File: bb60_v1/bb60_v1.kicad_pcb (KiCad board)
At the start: 2 copper layers, 281 x 94.4 mm, 145 parts, among them J1 Conn_01x04, SW1 SW_Push, SW2 SW_Push, U1 STM32F072CBTx, U2 XC6206PxxxMR, U3 USBLC6-2SC6

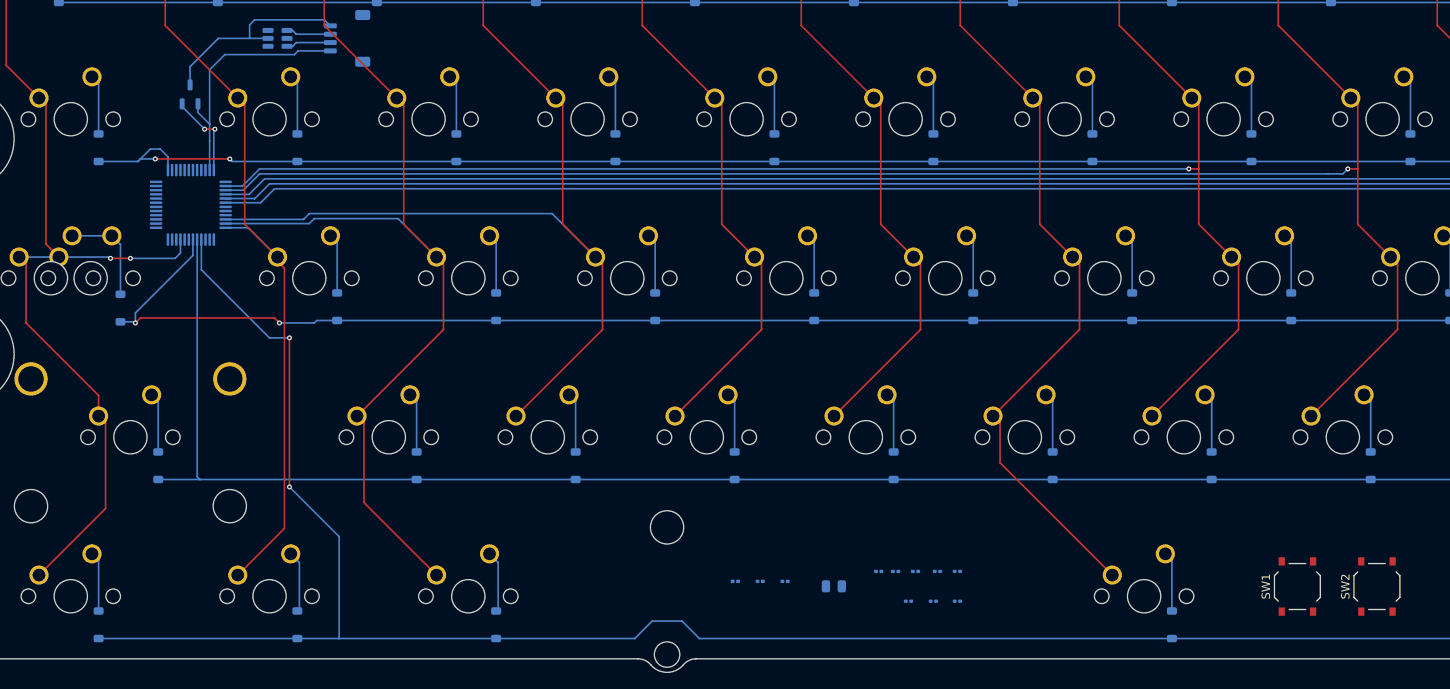
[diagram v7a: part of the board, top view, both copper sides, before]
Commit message: finished row/column traces
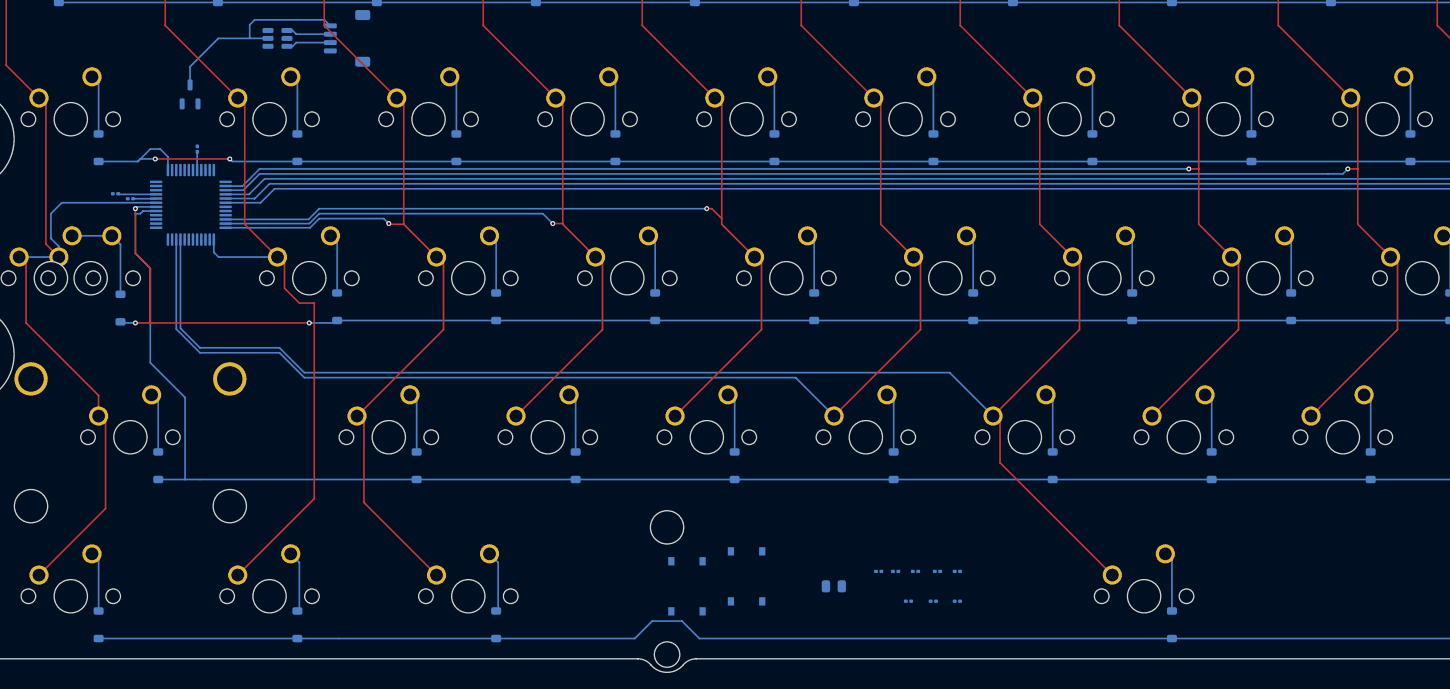
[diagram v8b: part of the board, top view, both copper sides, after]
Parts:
- SW1, SW2: moved to B.Cu
- moved R2 88.3 mm to (92.9, 107.0)
- moved R3 87.6 mm to (91.1, 106.4)
- moved R1 87.4 mm to (100.9, 101.0), turned to -90 degrees
- moved SW2 75.5 mm to (166.7, 152.2)
- moved SW1 73.1 mm to (159.5, 153.4)
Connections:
- U1 pad 10: /COL3 -> /COL4
- U1 pad 11: /COL2 -> /COL3
- U1 pad 12: /COL1 -> /COL2
- U1 pad 13: /COL6 -> /COL1
- U1 pad 14: /COL5 -> unconnected-(U1-PA4-Pad14)
- U1 pad 17: /ROW3 -> unconnected-(U1-PA7-Pad17)
- U1 pad 18: /ROW2 -> unconnected-(U1-PB0-Pad18)
- U1 pad 21: /COL0 -> /COL6
- U1 pad 22: unconnected-(U1-PB11-Pad22) -> /COL5
- U1 pad 29: unconnected-(U1-PA8-Pad29) -> /ROW3
- U1 pad 30: unconnected-(U1-PA9-Pad30) -> /ROW2
- U1 pad 31: unconnected-(U1-PA10-Pad31) -> /COL0
- U1 pad 43: /COL4 -> unconnected-(U1-PB7-Pad43)
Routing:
- net /COL6: track 92.7 -> 205.0 mm
- net /COL5: track 67.7 -> 161.5 mm
- net /COL4: track 67.7 -> 128.2 mm, vias 0 -> 1
- net /ROW4: track 316.7 -> 260.6 mm, vias 2 -> 0
- net GND: track 30.4 -> 0.00 mm
- net +3.3V: track 10.3 -> 0.00 mm, vias 2 -> 0
- net /ROW3: track 283.5 -> 291.6 mm
- net /COL1: track 92.4 -> 98.2 mm
- net /COL3: track 114.5 -> 109.1 mm, vias 0 -> 1
- net /COL2: track 118.1 -> 112.8 mm, vias 0 -> 1
- net /RES_D+: track 0.00 -> 4.58 mm
- net /ROW2: track 260.9 -> 264.6 mm, vias 2 -> 3
- net /RES_D-: track 0.00 -> 2.77 mm
- net /COL0: track 108.0 -> 110.3 mm, vias 2 -> 0
- net /BOOT0: track 0.00 -> 2.21 mm
